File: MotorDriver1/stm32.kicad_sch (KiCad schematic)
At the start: 31 parts, among them IC1 STM32C092RCT6, J1 GT-USB-7010ASV, SW1 K2-6639SP-C4SC-04, SW2 K2-6639SP-C4SC-04, SW3 K2-6639SP-C4SC-04, U1 TPS22916CNYFPR, U2 CH340X, Y1 48 MHz, Y2 32.768 kHz

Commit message: Re-layed out eo stuff
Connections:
- net USER_BTN: now also IC1.1 (PC11); no longer IC1.3 (PC13)
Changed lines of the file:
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@@
+	)
+	(no_connect
+		(at 119.38 85.09)
 	)
 	(no_connect
@@
 	)
 	(no_connect
-		(at 119.38 80.01)
-	)
-	(no_connect
 		(at 154.94 64.77)
 	)
@@
 	(wire
 		(pts
-			(xy 109.22 85.09) (xy 119.38 85.09)
-		)
-		(stroke
-			(width 0)
-			(type default)
-		)
-	)
-	(wire
-		(pts
 			(xy 22.86 41.91) (xy 33.02 41.91)
 		)
@@
 		(pts
 			(xy 22.86 41.91) (xy 22.86 45.72)
+		)
+		(stroke
+			(width 0)
+			(type default)
+		)
+	)
+	(wire
+		(pts
+			(xy 109.22 80.01) (xy 119.38 80.01)
 		)
 		(stroke
@@
 		)
 	)
-	(global_label "USER_BTN"
-		(shape input)
-		(at 109.22 85.09 180)
-		(fields_autoplaced yes)
-		(effects
-			(font
-				(size 1.27 1.27)
-			)
-			(justify right)
-		)
-		(property "Intersheetrefs" "${INTERSHEET_REFS}"
-			(at 96.7401 85.09 0)
-			(effects
-				(font
-					(size 1.27 1.27)
-				)
-				(justify right)
-				(hide yes)
-			)
-		)
-	)
 	(global_label "3V3"
 		(shape input)
@@
 				(hide yes)
 			)
+		)
+	)
+	(global_label "USER_BTN"
+		(shape input)
+		(at 109.22 80.01 180)
+		(fields_autoplaced yes)
+		(effects
+			(font
+				(size 1.27 1.27)
+			)
+			(justify right)
+		)
+		(property "Intersheetrefs" "${INTERSHEET_REFS}"
+			(at 96.7401 80.01 0)
+			(effects
+				(font
+					(size 1.27 1.27)
+				)
+				(justify right)
+				(hide yes)
+			)

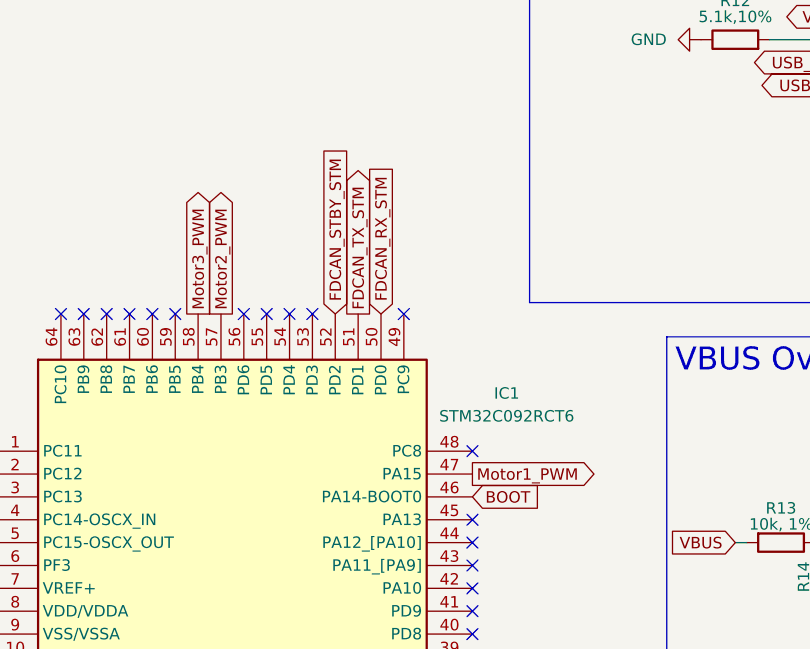
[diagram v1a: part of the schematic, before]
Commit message: component placing and first traces
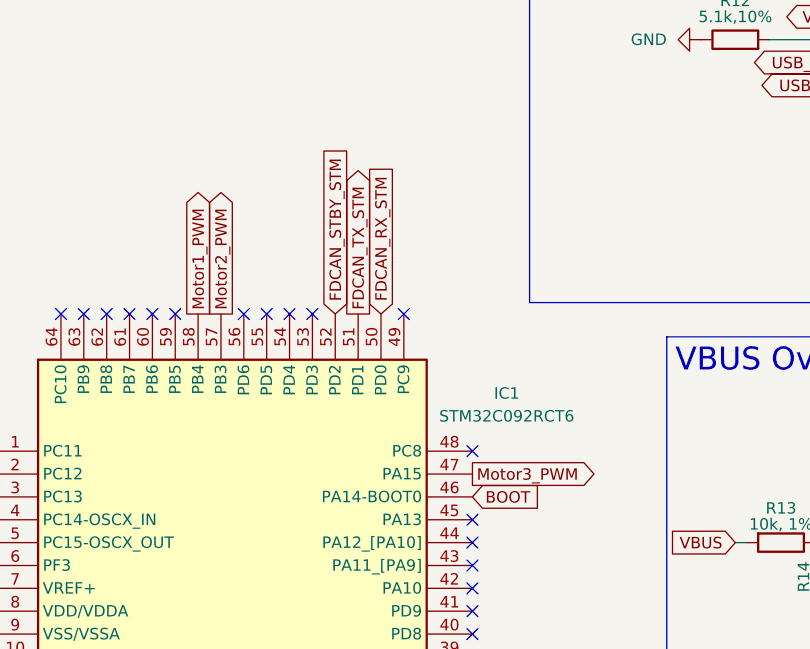
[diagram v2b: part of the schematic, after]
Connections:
- net Motor1_PWM: now also IC1.58 (PB4); no longer IC1.47 (PA15)
- net Motor3_PWM: now also IC1.47 (PA15); no longer IC1.58 (PB4)
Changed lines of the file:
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@@
 		)
 	)
-	(global_label "Motor1_PWM"
+	(global_label "Motor3_PWM"
 		(shape output)
 		(at 172.72 82.55 0)
@@
 		)
 	)
-	(global_label "Motor3_PWM"
+	(global_label "Motor1_PWM"
 		(shape output)
 		(at 142.24 64.77 90)

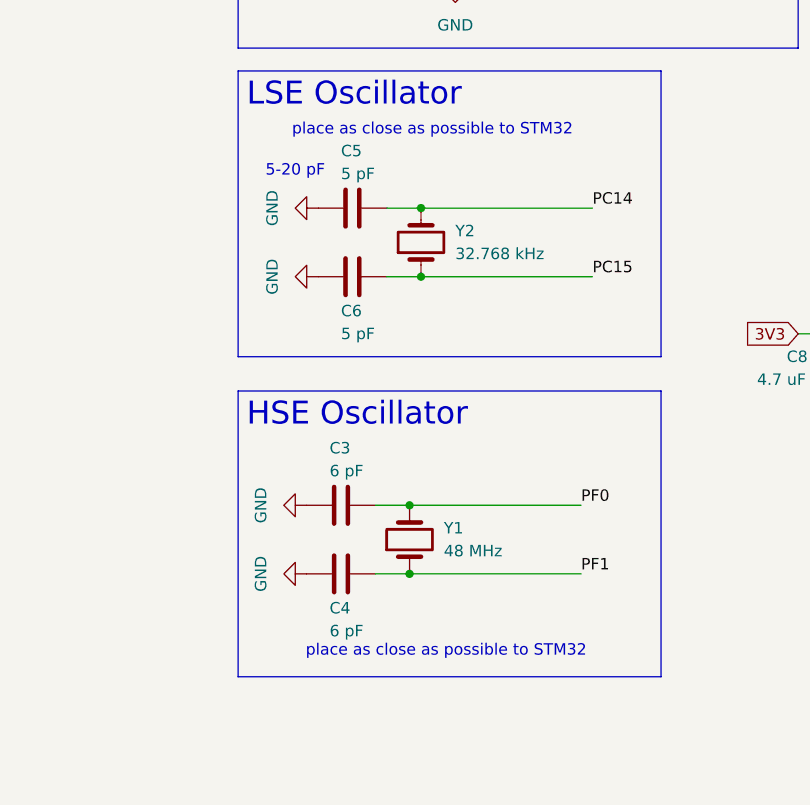
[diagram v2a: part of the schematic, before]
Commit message: Updated crystal footprints
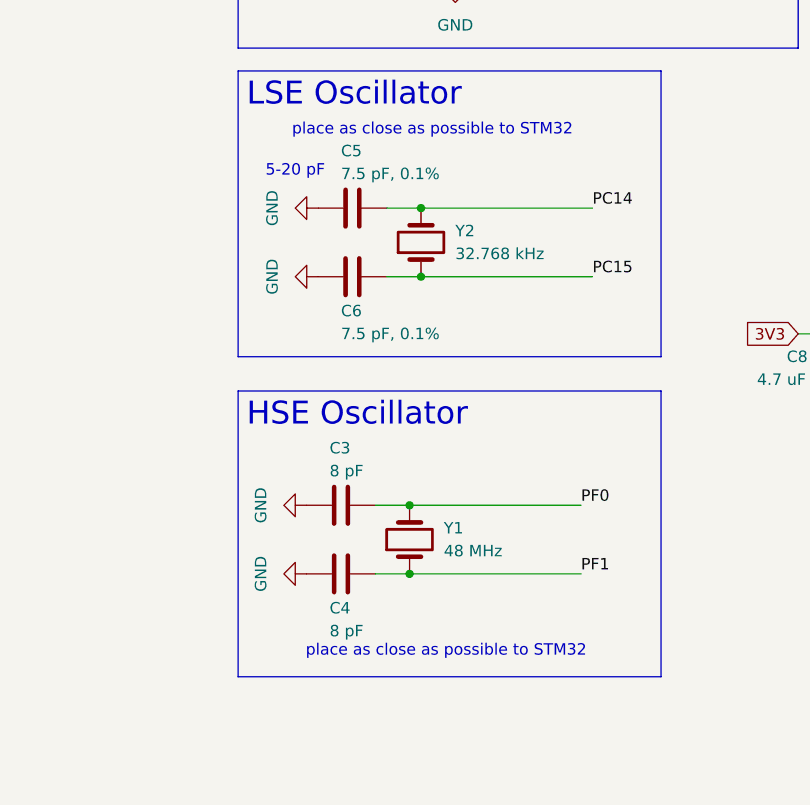
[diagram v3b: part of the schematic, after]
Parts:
- C3, C4: value 6 pF -> 8 pF
- C5, C6: value 5 pF -> 7.5 pF, 0.1%
- Y1: footprint footprintLib:XTAL_ECS-.327-12.5-12R-TR -> footprintLib:ECS-480-8-30-JGN-TR
- Y2: footprint footprintLib:XTAL_ECS-.327-12.5-12R-TR -> footprintLib:MU00527-32.768K
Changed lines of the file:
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@@
 			)
 		)
-		(property "Value" "5 pF"
+		(property "Value" "7.5 pF, 0.1%"
 			(at 26.67 97.7899 90)
 			(effects
@@
 			)
 		)
-		(property "Value" "6 pF"
+		(property "Value" "8 pF"
 			(at 25.4 130.8099 90)
 			(effects
@@
 			)
 		)
-		(property "Value" "5 pF"
+		(property "Value" "7.5 pF, 0.1%"
 			(at 26.67 80.0099 90)
 			(effects
@@
 			)
 		)
-		(property "Value" "6 pF"
+		(property "Value" "8 pF"
 			(at 25.4 113.0299 90)
 			(effects
@@
 			)
 		)
-		(property "Footprint" "footprintLib:XTAL_ECS-.327-12.5-12R-TR"
+		(property "Footprint" "footprintLib:ECS-480-8-30-JGN-TR"
 			(at 34.29 120.65 0)
 			(effects
@@
 			)
 		)
-		(property "Datasheet" "~CS08231-48M"
+		(property "Datasheet" "ECS-480-8-30-JGN-TR"
 			(at 34.29 120.65 0)
 			(effects
@@
 			)
 		)
-		(property "Description" "Two pin crystal, CS08231-48M"
+		(property "Description" "Two pin crystal, ECS-480-8-30-JGN-TR"
 			(at 34.29 120.65 0)
 			(effects
@@
 			)
 		)
-		(property "Footprint" "footprintLib:XTAL_ECS-.327-12.5-12R-TR"
+		(property "Footprint" "footprintLib:MU00527-32.768K"
 			(at 35.56 87.63 0)
 			(effects
@@
 			)
 		)
-		(property "Description" "Two pin crystal, ECS-.327-12.5-12R-TR"
+		(property "Description" "Two pin crystal, MU00527-32.768K"
 			(at 35.56 87.63 0)
 			(effects

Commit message: Exported final JLCPCB files
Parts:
- removed R13, R14: 10k, 1%, Resistor_SMD:R_0402_1005Metric, symbol Device:R
- removed U1: TPS22916CNYFPR, footprintLib:TPS22916CNYFPR, symbol pcb:TPS22916CNYFPR
- added U1: NCP361SNT1G, footprintLib:SOT95P275X110-5N, symbol pcb:NCP361SNT1G
- C10, C12: value 100nF -> 100 nF
- C11, C5, C6: footprint Capacitor_SMD:C_0201_0603Metric -> Capacitor_SMD:C_0402_1005Metric
- C13: value 100nF -> 1 uF; footprint Capacitor_SMD:C_0402_1005Metric -> Capacitor_SMD:C_0603_1608Metric
- C14: value 10uF -> 1 uF; footprint Capacitor_SMD:C_1206_3216Metric -> Capacitor_SMD:C_0603_1608Metric
- C3, C4: value 8 pF -> 8 pF, 0.1%; footprint Capacitor_SMD:C_0201_0603Metric -> Capacitor_SMD:C_0402_1005Metric
- D5, D6, D7: value ESDALC6V1-1U2 -> ESDALC6V1-1M2; footprint Diode_SMD:D_0201_0603Metric -> Diode_SMD:D_0402_1005Metric
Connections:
- net 3V3: no longer SW3.1
- net 5V_USB: now also U1.5 (OUT); no longer C13.2
- net BOOT: no longer SW3.3
- net GND: now also U1.2 (GND), U1.3 (~{EN}); no longer SW2.1
- net NRST: no longer SW2.3
- net USER_BTN: no longer SW1.3
- net VBUS: now also C13.2, U1.1 (IN)
- net at R9.2, SW1.2: no longer SW1.1
- no-connect marks 45 -> 52
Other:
- moved on the sheet: C13
